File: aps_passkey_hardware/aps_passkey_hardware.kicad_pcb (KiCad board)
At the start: 2 copper layers, 34 parts, among them J1 USB_A, SW1 SW_Push, U1 RP2354A-QFN60, U2 TLV75512PDQNR, Y1 Crystal_GND24

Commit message: new design
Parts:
- added U3: W25Q128JVS, Package_SO:SOIC-8_5.3x5.3mm_P1.27mm, F.Cu at (89.8, 70.5)
- moved R5 50.4 mm to (94.1, 88.5), turned to 180 degrees
- moved C5 43.7 mm to (96.9, 91.0), turned to -90 degrees
- moved C20 26.9 mm to (89.7, 77.5)
- moved U1 26.9 mm to (94.3, 83.1)
- moved Y1 26.9 mm to (94.4, 91.0), turned to 180 degrees
- moved C1 26.9 mm to (96.2, 78.1)
- moved U2 26.9 mm to (90.7, 75.9)
- moved L1 26.7 mm to (96.7, 76.3)
- moved J1 26.6 mm to (93.6, 63.1)
- moved C15 21.0 mm to (119.8, 64.7)
- moved C16 21.0 mm to (119.8, 66.7)
- moved C17 21.0 mm to (119.8, 68.6)
- moved C18 21.0 mm to (119.8, 70.6)
- moved C21 21.0 mm to (119.8, 72.6)
- moved C10 21.0 mm to (116.9, 68.6)
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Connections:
- C4 pad 1: Net-(C4-Pad1) -> XIN
- C5 pad 1: Net-(C5-Pad1) -> XOUT
- U1 pad 55: unconnected-(U1-QSPI_SD3-Pad55) -> SD3
- U1 pad 56: unconnected-(U1-QSPI_SCLK-Pad56) -> QSPI_SCLK
- U1 pad 57: unconnected-(U1-QSPI_SD0-Pad57) -> SD0
- U1 pad 58: unconnected-(U1-QSPI_SD2-Pad58) -> SD2
- U1 pad 59: unconnected-(U1-QSPI_SD1-Pad59) -> SD1
- Y1 pad 1: Net-(C4-Pad1) -> XIN
- Y1 pad 3: Net-(C5-Pad1) -> XOUT
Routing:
- net Net-(J1-VBUS): track 8.22 -> 0.00 mm
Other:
- board outline added: 19.1 x 2 mm

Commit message: New Design
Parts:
- added U4: W25Q128JVP, Package_SON:WSON-8-1EP_6x5mm_P1.27mm_EP3.4x4.3mm, F.Cu at (3.77, 2.85)
- U1: value RP2354A-QFN60 -> RP2350A-QFN60
- moved C16 34.4 mm to (88.5, 81.0), turned to -90 degrees
- moved R6 33.6 mm to (89.2, 87.0), turned to -90 degrees
- moved SW1 30.8 mm to (98.7, 86.4), turned to 90 degrees
- moved C10 30.3 mm to (88.5, 79.2), turned to 90 degrees
- moved D1 30.2 mm to (89.0, 84.5), turned to 90 degrees
- moved R2 29.8 mm to (94.1, 67.6), turned to 90 degrees
- moved C9 29.6 mm to (88.5, 75.2), turned to 90 degrees
- moved C21 29.6 mm to (90.9, 65.9), turned to -90 degrees
- moved R3 29.5 mm to (95.0, 67.6), turned to 90 degrees
- moved C8 29.1 mm to (94.8, 83.5)
- moved C4 29.0 mm to (90.1, 87.0), turned to 90 degrees
- moved C11 28.6 mm to (91.4, 83.5), turned to 180 degrees
- moved C13 27.4 mm to (91.4, 84.4), turned to 180 degrees
- moved C15 26.5 mm to (98.6, 80.6), turned to -90 degrees
- moved C7 25.5 mm to (88.5, 77.2), turned to 90 degrees
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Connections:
- net DM renamed D-
- net DP renamed D+
- net Net-(U1-USB_DM) renamed /TR-
- net Net-(U1-USB_DP) renamed /TR+
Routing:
- net /TR-: track 0.00 -> 7.22 mm
- net /TR+: track 0.00 -> 7.20 mm
- net Net-(J1-VBUS): track 0.00 -> 7.01 mm
- net +3V3: track 0.00 -> 2.63 mm
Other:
- board size 19.1 x 2 mm -> 12.1 x 35 mm

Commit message: pcb
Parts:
- removed U3: W25Q128JVS, Package_SO:SOIC-8_5.3x5.3mm_P1.27mm
- moved C21 8.27 mm to (83.8, 70.3)
- moved C20 8.27 mm to (85.0, 70.8)
- moved C18 6.65 mm to (91.3, 66.8), turned to -90 degrees
- moved C19 5.21 mm to (90.1, 66.7)
- moved U2 3.57 mm to (89.7, 69.5)
- moved C5 1.91 mm to (94.8, 84.5), turned to 0 degrees
- moved C14 1.51 mm to (92.8, 72.5)
- moved SW1 1.27 mm to (97.5, 86.3)
- moved C4 0.44 mm to (89.7, 87.0)
- moved R6 0.44 mm to (88.7, 87.0)
- moved Y1 0.39 mm to (92.3, 86.7)
- moved C13 0.36 mm to (91.0, 84.5)
- moved C11 0.36 mm to (91.0, 83.5)
- moved D1 0.27 mm to (88.7, 84.5)
- moved L1 0.17 mm to (96.4, 71.7)
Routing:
- net /TR-: track 7.22 -> 0.00 mm
- net /TR+: track 7.20 -> 0.00 mm
- net Net-(J1-VBUS): track 7.01 -> 1.10 mm

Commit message: PCB Done
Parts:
- removed U4: W25Q128JVP, Package_SON:WSON-8-1EP_6x5mm_P1.27mm_EP3.4x4.3mm
- moved C12 14.6 mm to (90.2, 70.5), turned to 90 degrees
- moved C17 8.81 mm to (91.1, 70.5)
- moved C19 8.76 mm to (98.8, 67.9), turned to 90 degrees
- moved C21 6.42 mm to (89.9, 68.1)
- moved C18 6.33 mm to (97.6, 67.5), turned to 90 degrees
- moved C20 4.53 mm to (88.7, 68.1)
- moved U2 2.97 mm to (91.9, 67.5)
- moved R2 2.77 mm to (93.2, 70.2)
- moved R3 2.77 mm to (94.1, 70.2)
- moved C1 2.74 mm to (95.7, 70.8)
- moved SW1 2.51 mm to (97.3, 83.8)
- moved C10 2.50 mm to (88.5, 76.7)
- moved C11 2.50 mm to (91.0, 81.0)
- moved C13 2.50 mm to (91.0, 82.0)
- moved C15 2.50 mm to (98.6, 78.1)
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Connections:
- U1 pad 15: unconnected-(U1-GPIO11-Pad15) -> Net-(D1-A)
- U1 pad 37: Net-(D1-A) -> unconnected-(U1-GPIO25-Pad37)
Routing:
- net +3V3: track 2.63 -> 55.3 mm, vias 0 -> 9
- net +1V1: track 0.24 -> 25.5 mm
- net GND: track 0.00 -> 18.2 mm, vias 0 -> 29
- net QSPI_SS: track 0.00 -> 14.2 mm, vias 0 -> 2
- net D-: track 0.00 -> 11.7 mm, vias 0 -> 2
- net Net-(J1-VBUS): track 1.10 -> 12.6 mm
- net D+: track 0.00 -> 11.1 mm
- net XIN: track 0.01 -> 7.75 mm
- net Net-(U1-VREG_LX): track 0.00 -> 4.34 mm
- net Net-(U1-VREG_AVDD): track 0.00 -> 3.44 mm
- net Net-(D1-A): track 0.00 -> 3.02 mm
- net XOUT: track 0.00 -> 2.25 mm
- net /TR+: track 0.00 -> 2.14 mm
- net /TR-: track 0.00 -> 1.92 mm
- net Net-(R4-Pad1): track 0.00 -> 1.72 mm
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- added copper zone on B.Cu, net GND
- added copper zone on F.Cu, net GND
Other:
- board size 12.1 x 35 mm -> 12.1 x 33.3 mm

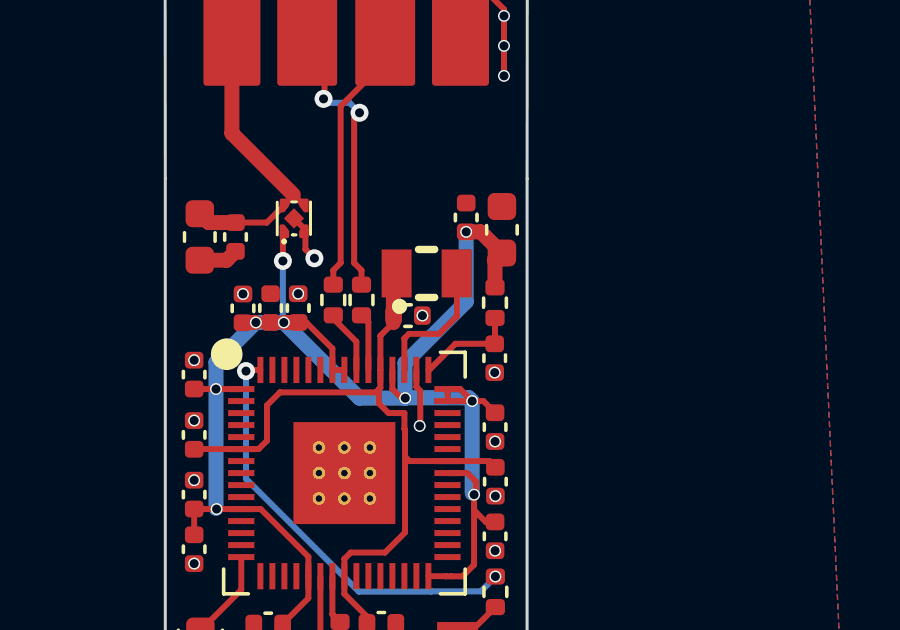
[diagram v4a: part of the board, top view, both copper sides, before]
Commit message: added silkscreen+panelisation part
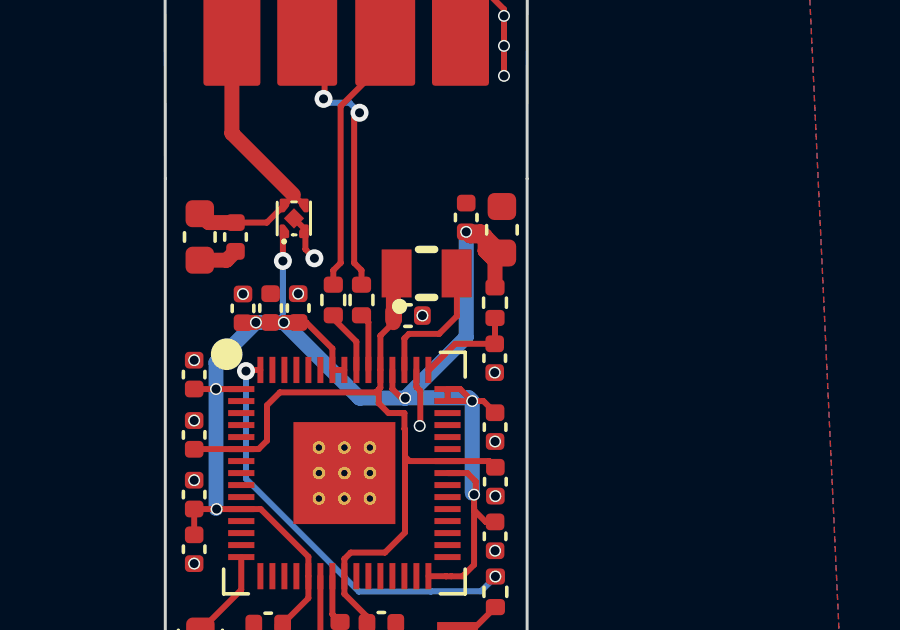
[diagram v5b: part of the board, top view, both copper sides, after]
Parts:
- added G***: LOGO, LOGO, B.Cu at (92.3, 63.8)
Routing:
- net +3V3: track 55.3 -> 57.3 mm
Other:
- board text added: "@ APSM!"

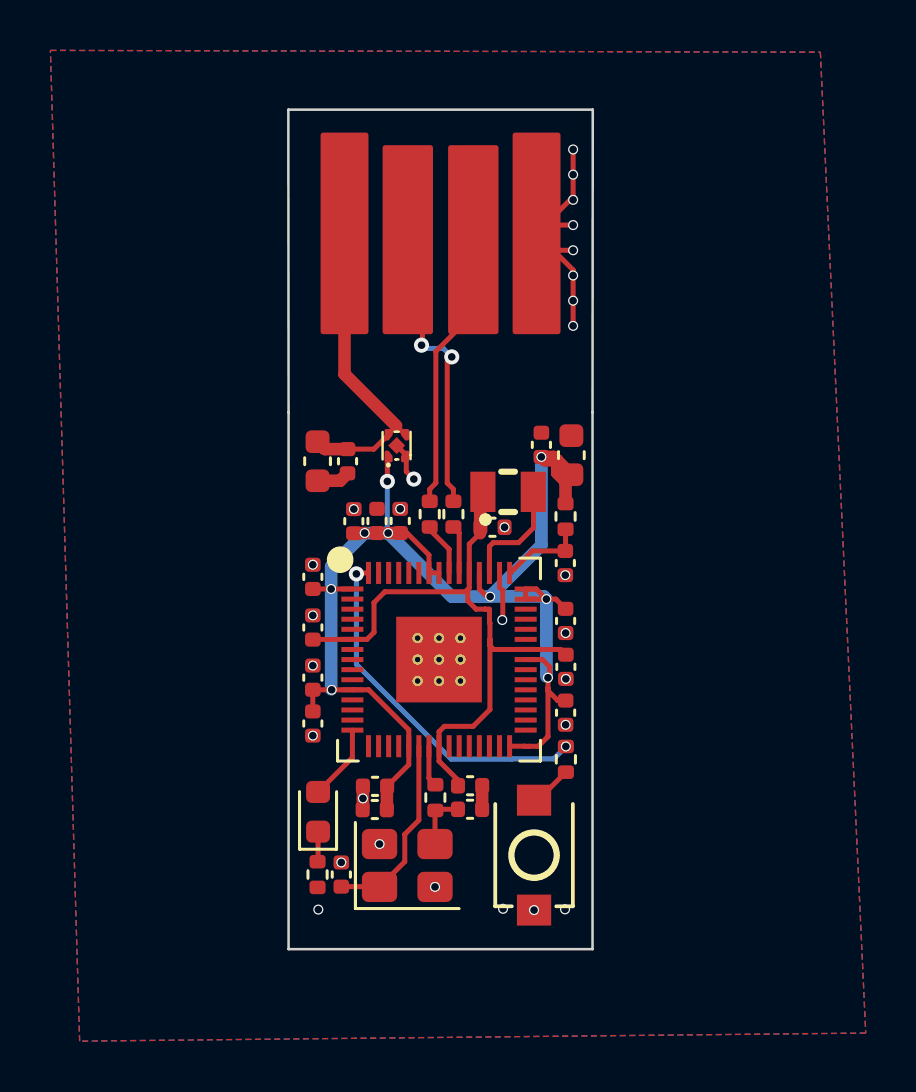
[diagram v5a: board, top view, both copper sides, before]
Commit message: fixed ground errors
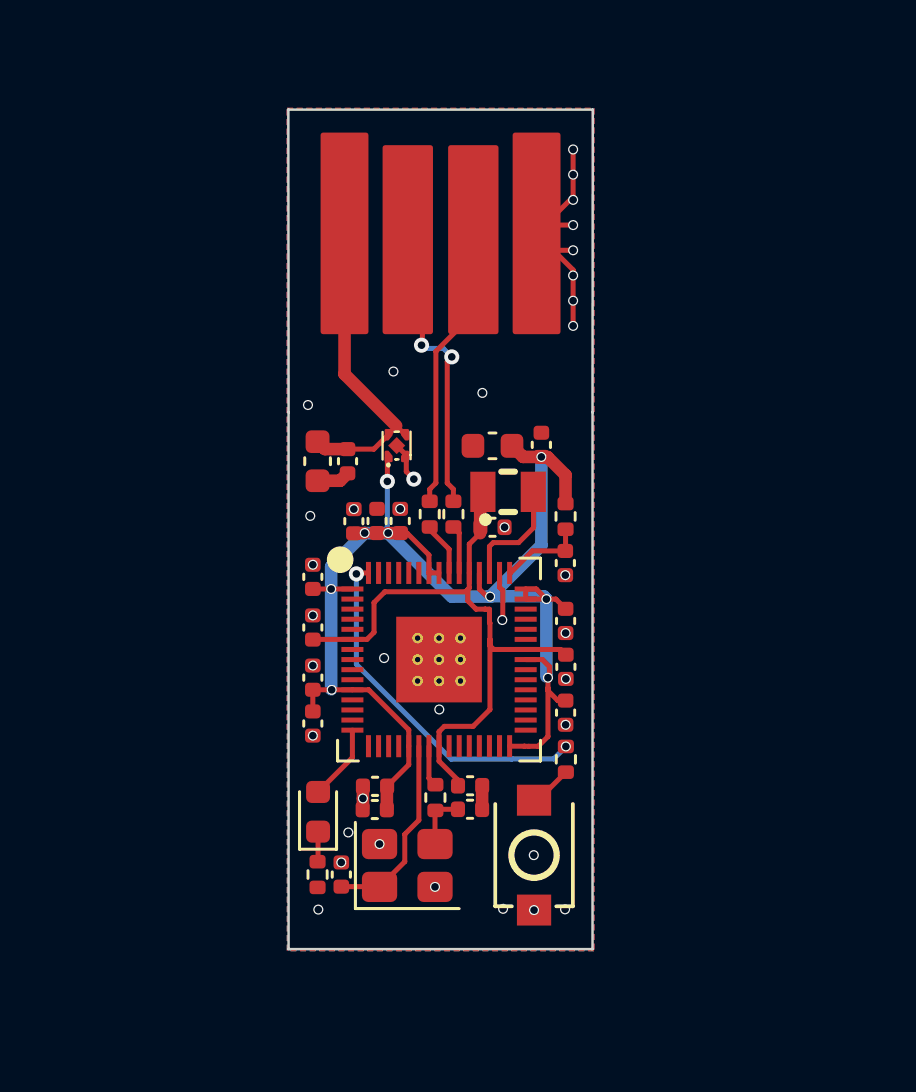
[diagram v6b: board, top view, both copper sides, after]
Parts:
- moved C19 3.15 mm to (95.7, 67.5), turned to 180 degrees
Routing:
- net +3V3: track 57.3 -> 56.3 mm
- net GND: vias 29 -> 37
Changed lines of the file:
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@@
 	(footprint "Capacitor_SMD:C_0603_1608Metric"
 		(layer "F.Cu")
-		(at 98.79 67.9 90)
+		(at 95.66 67.53 180)
 		(descr "Capacitor SMD 0603 (1608 Metric), square (rectangular) end terminal, IPC-7351 nominal, (Body size source: IPC-SM-782 page 76, https://www.pcb-3d.com/wordpress/wp-content/uploads/ipc-sm-782a_amendment_1_and_2.pdf), generated with kicad-footprint-generator")
 		(tags "capacitor")
 		(property "Reference" "C19"
-			(at 0 -1.43 90)
+			(at 0 -1.43 0)
 			(layer "F.SilkS")
 			(hide yes)
@@
 		)
 		(property "Value" "10u"
-			(at 0 1.43 90)
+			(at 0 1.43 0)
 			(layer "F.Fab")
 			(effects
@@
 		)
 		(property "Datasheet" ""
-			(at 0 0 90)
+			(at 0 0 0)
 			(layer "F.Fab")
 			(hide yes)
@@
 		)
 		(property "Description" "Unpolarized capacitor"
-			(at 0 0 90)
+			(at 0 0 0)
 			(layer "F.Fab")
 			(hide yes)
@@
 		(attr smd)
 		(fp_line
-			(start -0.14058 -0.51)
-			(end 0.14058 -0.51)
+			(start -0.14058 0.51)
+			(end 0.14058 0.51)
 			(stroke
 				(width 0.12)
@@
 		)
 		(fp_line
-			(start -0.14058 0.51)
-			(end 0.14058 0.51)
+			(start -0.14058 -0.51)
+			(end 0.14058 -0.51)
 			(stroke
 				(width 0.12)
@@
 		)
 		(fp_line
-			(start 1.48 -0.73)
-			(end 1.48 0.73)
+			(start 1.48 0.73)
+			(end -1.48 0.73)
 			(stroke
 				(width 0.05)
@@
 		)
 		(fp_line
-			(start -1.48 -0.73)
-			(end 1.48 -0.73)
+			(start 1.48 -0.73)
+			(end 1.48 0.73)
 			(stroke
 				(width 0.05)
@@
 		)
 		(fp_line
-			(start 1.48 0.73)
-			(end -1.48 0.73)
+			(start -1.48 0.73)
+			(end -1.48 -0.73)
 			(stroke
 				(width 0.05)
@@
 		)
 		(fp_line
-			(start -1.48 0.73)
-			(end -1.48 -0.73)
+			(start -1.48 -0.73)
+			(end 1.48 -0.73)
 			(stroke
 				(width 0.05)
@@
 		)
 		(fp_line
-			(start 0.8 -0.4)
-			(end 0.8 0.4)
+			(start 0.8 0.4)
+			(end -0.8 0.4)
 			(stroke
 				(width 0.1)
@@
 		)
 		(fp_line
-			(start -0.8 -0.4)
-			(end 0.8 -0.4)
+			(start 0.8 -0.4)
+			(end 0.8 0.4)
 			(stroke
 				(width 0.1)
@@
 		)
 		(fp_line
-			(start 0.8 0.4)
-			(end -0.8 0.4)
+			(start -0.8 0.4)
+			(end -0.8 -0.4)
 			(stroke
 				(width 0.1)
@@
 		)
 		(fp_line
-			(start -0.8 0.4)
-			(end -0.8 -0.4)
+			(start -0.8 -0.4)
+			(end 0.8 -0.4)
 			(stroke
 				(width 0.1)
@@
 		)
 		(fp_text user "${REFERENCE}"
-			(at 0 0 90)
+			(at 0 0 0)
 			(layer "F.Fab")
 			(effects
@@
 		)
 		(pad "1" smd roundrect
-			(at -0.775 0 90)
+			(at -0.775 0 180)
 			(size 0.9 0.95)
 			(layers "F.Cu" "F.Mask" "F.Paste")
@@
 		)
 		(pad "2" smd roundrect
-			(at 0.775 0 90)
+			(at 0.775 0 180)
 			(size 0.9 0.95)
 			(layers "F.Cu" "F.Mask" "F.Paste")
@@
 			(fill yes)
 			(layer "B.SilkS")
-			(net 787277472)
 		)
 		(fp_poly
@@
 			(fill yes)
 			(layer "B.SilkS")
-			(net 787277472)
 		)
 		(fp_poly
@@
 			(fill yes)
 			(layer "B.SilkS")
-			(net 787277472)
 		)
 		(fp_poly
@@
 			(fill yes)
 			(layer "B.SilkS")
-			(net 787277472)
 		)
 		(embedded_fonts no)
@@
 	)
 	(via
+		(at 88.34 65.91)
+		(size 0.4)
+		(drill 0.3)
+		(layers "F.Cu" "B.Cu")
+		(free yes)
+		(net 6)
+	)
+	(via
+		(at 91.73 64.58)
+		(size 0.4)
+		(drill 0.3)
+		(layers "F.Cu" "B.Cu")
+		(free yes)
+		(net 6)
+	)
+	(via
 		(at 97.31 85.95)
 		(size 0.4)
@@
 	)
 	(via
+		(at 91.36 75.95)
+		(size 0.4)
+		(drill 0.3)
+		(layers "F.Cu" "B.Cu")
+		(free yes)
+		(net 6)
+	)
+	(via
 		(at 92 70.03)
 		(size 0.4)
@@
 	)
 	(via
+		(at 88.43 70.31)
+		(size 0.4)
+		(drill 0.3)
+		(layers "F.Cu" "B.Cu")
+		(free yes)
+		(net 6)
+	)
+	(via
 		(at 98.5725 76.7775)
 		(size 0.4)
@@
 	)
 	(via
+		(at 93.55 77.99)
+		(size 0.4)
+		(drill 0.3)
+		(layers "F.Cu" "B.Cu")
+		(free yes)
+		(net 6)
+	)
+	(via
 		(at 96.14 70.76)
 		(size 0.4)
@@
 	)
 	(via
+		(at 97.3 83.77)
+		(size 0.4)
+		(drill 0.3)
+		(layers "F.Cu" "B.Cu")
+		(free yes)
+		(net 6)
+	)
+	(via
 		(at 88.5325 79.0275)
 		(size 0.4)
@@
 	)
 	(via
+		(at 95.26 65.43)
+		(size 0.4)
+		(drill 0.3)
+		(layers "F.Cu" "B.Cu")
+		(free yes)
+		(net 6)
+	)
+	(via
 		(at 98.86 56.77)
 		(size 0.4)
@@
 		(net 6)
 	)
+	(via
+		(at 89.94 82.87)
+		(size 0.4)
+		(drill 0.3)
+		(layers "F.Cu" "B.Cu")
+		(free yes)
+		(net 6)
+	)
 	(segment
 		(start 90.1025 78.81)
@@
 	)
 	(segment
-		(start 98.231 68.601)
-		(end 98.231 68.104)
+		(start 98.56 68.69)
+		(end 98.56 69.82)
 		(width 0.5)
 		(layer "F.Cu")
@@
 	)
 	(segment
-		(start 98.56 68.905)
-		(end 98.79 68.675)
-		(width 0.2)
+		(start 97.6 67.97)
+		(end 96.875 67.97)
+		(width 0.5)
 		(layer "F.Cu")
 		(net 20)
@@
 	)
 	(segment
-		(start 98.56 68.93)
-		(end 98.231 68.601)
-		(width 0.5)
-		(layer "F.Cu")
-		(net 20)
-	)
-	(segment
-		(start 98.085 67.97)
-		(end 98.79 68.675)
+		(start 97.84 67.97)
+		(end 98.56 68.69)
 		(width 0.5)
 		(layer "F.Cu")
@@
 	)
 	(segment
-		(start 97.734 68.104)
-		(end 97.6 67.97)
+		(start 96.875 67.97)
+		(end 96.435 67.53)
 		(width 0.5)
 		(layer "F.Cu")
@@
 	)
 	(segment
-		(start 98.535 68.905)
-		(end 98.56 68.905)
-		(width 0.5)
-		(layer "F.Cu")
-		(net 20)
-	)
-	(segment
 		(start 90.59 70.99)
 		(end 90.17 70.99)
@@
 	)
 	(segment
-		(start 98.56 69.82)
-		(end 98.56 68.93)
-		(width 0.5)
-		(layer "F.Cu")
-		(net 20)
-	)
-	(segment
 		(start 92.27 70.99)
 		(end 92.04 70.99)
@@
 	)
 	(segment
+		(start 97.6 67.97)
+		(end 97.84 67.97)
+		(width 0.5)
+		(layer "F.Cu")
+		(net 20)
+	)
+	(segment
 		(start 88.5325 78.0675)
 		(end 88.5325 77.2075)
@@
 	)
 	(segment
-		(start 98.231 68.601)
-		(end 98.535 68.905)
-		(width 0.5)
-		(layer "F.Cu")
-		(net 20)
-	)
-	(segment
 		(start 90.1025 77.21)
 		(end 89.28 77.21)
@@
 	)
 	(segment
-		(start 97.6 67.97)
-		(end 98.085 67.97)
-		(width 0.5)
-		(layer "F.Cu")
-		(net 20)
-	)
-	(segment
-		(start 98.231 68.104)
-		(end 97.734 68.104)
-		(width 0.5)
-		(layer "F.Cu")
-		(net 20)
-	)
-	(segment
 		(start 96.9775 73.21)
 		(end 97.4 73.21)
@@
 			(thermal_gap 0.5)
 			(thermal_bridge_width 0.5)
+			(island_removal_mode 1)
+			(island_area_min 10)
 		)
 		(polygon
 			(pts
-				(xy 78.12 51.84) (xy 108.67 51.91) (xy 110.47 90.83) (xy 79.28 91.15)
+				(xy 87.51 54.14) (xy 99.69 54.14) (xy 99.69 87.56) (xy 87.52 87.56)
 			)
 		)
